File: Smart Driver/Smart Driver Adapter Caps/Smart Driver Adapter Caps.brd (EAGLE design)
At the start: 34.3 x 58.4 mm, 9 parts, among them U2 DRV8353HMRTATWQFN_HMRTAT_TEX-M

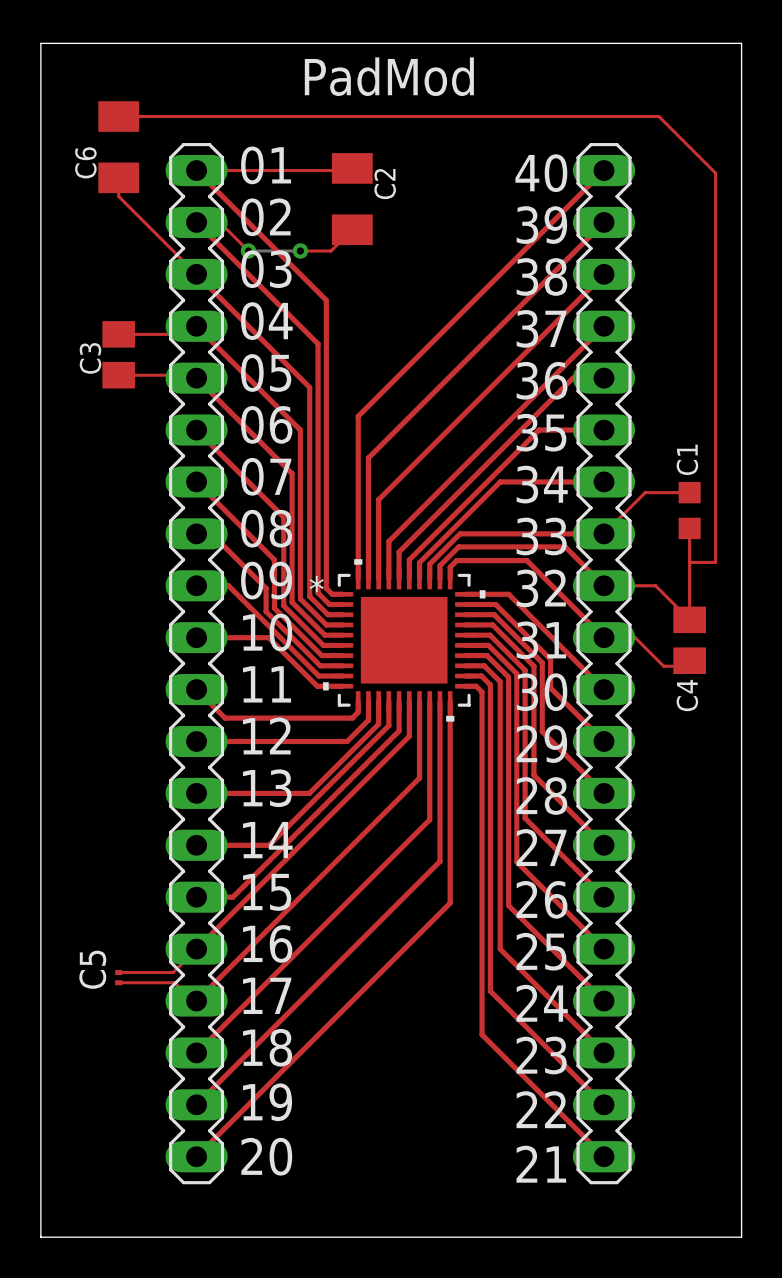
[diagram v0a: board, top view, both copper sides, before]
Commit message: Corrected Adapter with Caps PCB
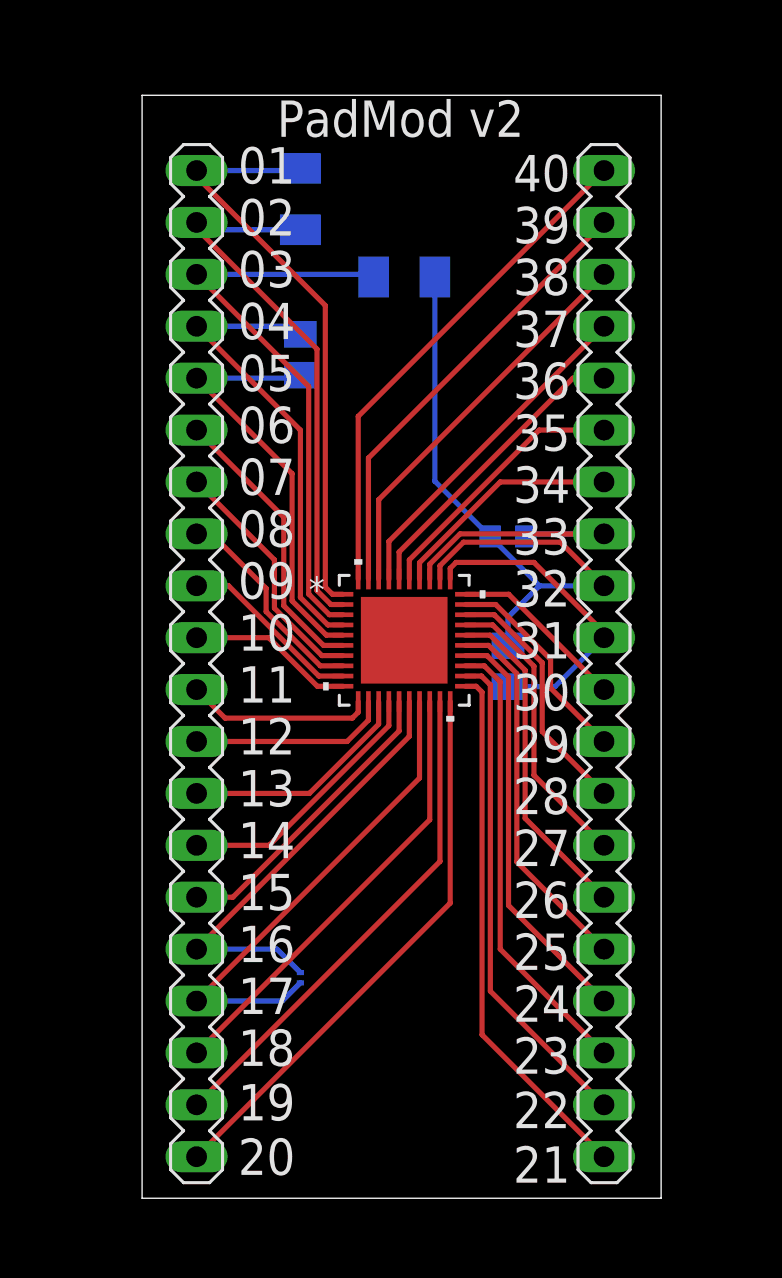
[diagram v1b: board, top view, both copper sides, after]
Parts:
- moved C6 15.3 mm to (17.8, 47.0), flipped to the bottom, turned to 180 degrees
- moved C1 8.98 mm to (22.9, 34.3), flipped to the bottom, turned to 0 degrees
- moved C4 8.98 mm to (22.9, 27.9), flipped to the bottom
- moved C3 8.89 mm to (12.7, 43.2), flipped to the bottom
- moved C5 8.89 mm to (12.7, 12.7), flipped to the bottom
- moved C2 2.54 mm to (12.7, 50.8), flipped to the bottom
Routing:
- net N$27: track 70.1 -> 34.0 mm
- net N$3: track 30.8 -> 27.2 mm, vias 2 -> 0
- net N$28: track 31.7 -> 29.1 mm
- net N$4: track 26.5 -> 28.7 mm
- net N$5: track 19.9 -> 21.2 mm
- net N$15: track 23.4 -> 24.6 mm
- net N$26: track 20.8 -> 22.0 mm
- net N$1: track 14.9 -> 13.7 mm
- net N$41: track 22.1 -> 23.3 mm
- net N$16: track 14.7 -> 15.5 mm
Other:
- board size 34.3 x 58.4 mm -> 25.4 x 54 mm
- board text added: "PadMod v2"
- board text removed: "PadMod"
